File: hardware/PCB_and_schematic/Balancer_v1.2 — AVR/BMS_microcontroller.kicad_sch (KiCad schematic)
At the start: 60 parts, among them J10 RS485, J2 VOLTAGE_3WIRE, J8 ICP, J9 RS485, Q17 BC817, Q19 BC817, Q20 BC817, Q21 BC817, Q22 BC817, U4 TL432DBZ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

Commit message: Add PWM code
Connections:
- net TEMP_HEAT_SINK_12V renamed DAC
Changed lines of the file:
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@@
 		)
 	)
-	(global_label "TEMP_HEAT_SINK_12V"
+	(global_label "DAC"
 		(shape input)
 		(at 72.39 86.36 180)
@@
 		)
 		(property "Intersheetrefs" "${INTERSHEET_REFS}"
-			(at 49.2059 86.36 0)
+			(at 65.7762 86.36 0)
 			(effects
 				(font

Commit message: New schematic BMS
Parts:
- added C4: 100n, Capacitor_SMD:C_0805_2012Metric_Pad1.18x1.45mm_HandSolder, symbol Device:C
- added R12: 10k, Resistor_SMD:R_0805_2012Metric_Pad1.20x1.40mm_HandSolder, symbol Device:R
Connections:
- net +5V: now also C4.1, R12.1
- net UPDI: now also C4.2, R12.2
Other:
- moved on the sheet: C19, C22, C23, J8, R47, R94, U4

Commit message: Update electrical schematic and BMS schematic
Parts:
- removed J8: ICP, Connector_PinHeader_2.54mm:PinHeader_1x06_P2.54mm_Vertical, symbol Connector_Generic:Conn_01x06
- added J16: ICP, Connector_PinHeader_2.54mm:PinHeader_1x05_P2.54mm_Vertical, symbol Connector_Generic:Conn_01x05
- added Q23: BC817, Package_TO_SOT_SMD:SOT-23, symbol Transistor_BJT:BC817
- added R42, R64: 1k, Resistor_SMD:R_0805_2012Metric_Pad1.20x1.40mm_HandSolder, symbol Device:R
- added R65: 4k7, Resistor_SMD:R_0805_2012Metric_Pad1.20x1.40mm_HandSolder, symbol Device:R
- added U10: PC817, Package_DIP:DIP-4_W7.62mm, symbol Isolator:PC817
- added U5: ADUM3211ARZ, R_8_ADI, symbol My-Lib:ADUM3211ARZ
- added U9: B0505S-1W, My-Footprints:B0505S, symbol My-Lib:B0505S-1W
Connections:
- net +5V: now also J16.2 (Pin_2), U10.1, U5.1 (VDD1), U9.1 (GND); no longer J10.1 (Pin_1), J9.1 (Pin_1), R51.1, U6.8 (VCC)
- net DBG_UART: now also J16.5 (Pin_5)
- net GND: now also J16.3 (Pin_3), Q23.2 (E), U5.4 (GND1), U9.2 (VIN); no longer C20.2, D16.1 (A1), D17.1 (A1), J10.4 (Pin_4), J9.4 (Pin_4), R53.2, U6.5 (GND)
- net RS232_RX: now also U5.2 (VOA); no longer U6.1 (RO)
- net RS232_TX: now also U5.3 (VIB); no longer U6.4 (DI)
- net RS485_OUTPUT_ENABLE: now also R64.1; no longer U6.2 (~{RE}), U6.3 (DE)
- net RST: now also J16.1 (Pin_1)
- net UPDI: now also J16.4 (Pin_4)
- new net: Q23.1 (B), R64.2
- new net: Q23.3 (C), R42.1
- new net: R65.2, U10.4, U6.2 (~{RE}), U6.3 (DE)
- new net: U5.7 (VIA), U6.1 (RO)
- new net: U5.6 (VOB), U6.4 (DI)
- new net: R42.2, U10.2
- new net +5V_RS485: J10.1 (Pin_1), J9.1 (Pin_1), R51.1, R65.1, U5.8 (VDD2), U6.8 (VCC), U9.4 (VOUT)
- new net GND_RS485: C20.2, D16.1 (A1), D17.1 (A1), J10.4 (Pin_4), J9.4 (Pin_4), R53.2, U10.3, U5.5 (GND2), U6.5 (GND), U9.3 (0V)
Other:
- moved on the sheet: C17, C18, C20, C21, C24, C25, D15, D16, D17, D18, D19, D20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

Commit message: Balancer PCB update
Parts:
- added C32: 100n, Capacitor_SMD:C_0805_2012Metric_Pad1.18x1.45mm_HandSolder, symbol Device:C
- U5: footprint R_8_ADI -> Package_SO:SO-8_3.9x4.9mm_P1.27mm
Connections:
- net +5V: no longer C20.1
- net +5V_RS485: now also C20.1, C32.1
- net GND_RS485: now also C32.2
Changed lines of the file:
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@@
 	)
 	(symbol
+		(lib_id "Device:C")
+		(at 273.05 102.87 0)
+		(unit 1)
+		(exclude_from_sim no)
+		(in_bom yes)
+		(on_board yes)
+		(dnp no)
+		(property "Reference" "C32"
+			(at 265.43 101.854 0)
+			(effects
+				(font
+					(size 1.27 1.27)
+				)
+				(justify left)
+			)
+		)
+		(property "Value" "100n"
+			(at 265.43 104.14 0)
+			(effects
+				(font
+					(size 1.27 1.27)
+				)
+				(justify left)
+			)
+		)
+		(property "Footprint" "Capacitor_SMD:C_0805_2012Metric_Pad1.18x1.45mm_HandSolder"
+			(at 274.0152 106.68 0)
+			(effects
+				(font
+					(size 1.27 1.27)
+				)
+				(hide yes)
+			)
+		)
+		(property "Datasheet" "~"
+			(at 273.05 102.87 0)
+			(effects
+				(font
+					(size 1.27 1.27)
+				)
+				(hide yes)
+			)
+		)
+		(property "Description" "Unpolarized capacitor"
+			(at 273.05 102.87 0)
+			(effects
+				(font
+					(size 1.27 1.27)
+				)
+				(hide yes)
+			)
+		)
+		(pin "2"
+		)
+		(pin "1"
+		)
+		(instances
+			(project "Balancer"
+				(path "/555ba40f-9abb-4b99-82c6-07e888fda9fd/3b90ff07-e5cb-404b-939d-de320e975ba1"
+					(reference "C32")
+					(unit 1)
+				)
+			)
+		)
+	)
+	(symbol
 		(lib_id "Device:R")
 		(at 34.29 123.19 0)
@@
 	)
 	(symbol
+		(lib_id "power:+5V")
+		(at 273.05 74.93 0)
+		(unit 1)
+		(exclude_from_sim no)
+		(in_bom yes)
+		(on_board yes)
+		(dnp no)
+		(fields_autoplaced yes)
+		(property "Reference" "#PWR072"
+			(at 273.05 78.74 0)
+			(effects
+				(font
+					(size 1.27 1.27)
+				)
+				(hide yes)
+			)
+		)
+		(property "Value" "+5V_RS485"
+			(at 273.05 69.85 0)
+			(effects
+				(font
+					(size 1.27 1.27)
+				)
+			)
+		)
+		(property "Footprint" ""
+			(at 273.05 74.93 0)
+			(effects
+				(font
+					(size 1.27 1.27)
+				)
+				(hide yes)
+			)
+		)
+		(property "Datasheet" ""
+			(at 273.05 74.93 0)
+			(effects
+				(font
+					(size 1.27 1.27)
+				)
+				(hide yes)
+			)
+		)
+		(property "Description" "Power symbol creates a global label with name \"+5V\""
+			(at 273.05 74.93 0)
+			(effects
+				(font
+					(size 1.27 1.27)
+				)
+				(hide yes)
+			)
+		)
+		(pin "1"
+		)
+		(instances
+			(project "Balancer"
+				(path "/555ba40f-9abb-4b99-82c6-07e888fda9fd/3b90ff07-e5cb-404b-939d-de320e975ba1"
+					(reference "#PWR072")
+					(unit 1)
+				)
+			)
+		)
+	)
+	(symbol
 		(lib_id "My-Lib:ADUM3211ARZ")
 		(at 219.71 54.61 0)
@@
 			)
 		)
-		(property "Footprint" "R_8_ADI"
+		(property "Footprint" "Package_SO:SO-8_3.9x4.9mm_P1.27mm"
 			(at 223.266 53.34 0)
 			(effects
@@
 	)
 	(symbol
-		(lib_id "power:+5V")
-		(at 273.05 74.93 0)
-		(unit 1)
-		(exclude_from_sim no)
-		(in_bom yes)
-		(on_board yes)
-		(dnp no)
-		(fields_autoplaced yes)
-		(property "Reference" "#PWR072"
-			(at 273.05 78.74 0)
-			(effects
-				(font
-					(size 1.27 1.27)
-				)
-				(hide yes)
-			)
-		)
-		(property "Value" "+5V"
-			(at 273.05 69.85 0)
-			(effects
-				(font
-					(size 1.27 1.27)
-				)
-			)
-		)
-		(property "Footprint" ""
-			(at 273.05 74.93 0)
-			(effects
-				(font
-					(size 1.27 1.27)
-				)
-				(hide yes)
-			)
-		)
-		(property "Datasheet" ""
-			(at 273.05 74.93 0)
-			(effects
-				(font
-					(size 1.27 1.27)
-				)
-				(hide yes)
-			)
-		)
-		(property "Description" "Power symbol creates a global label with name \"+5V\""
-			(at 273.05 74.93 0)
-			(effects
-				(font
-					(size 1.27 1.27)
-				)
-				(hide yes)
-			)
-		)
-		(pin "1"
-		)
-		(instances
-			(project "Balancer"
-				(path "/555ba40f-9abb-4b99-82c6-07e888fda9fd/3b90ff07-e5cb-404b-939d-de320e975ba1"
-					(reference "#PWR072")
-					(unit 1)
-				)
-			)
-		)
-	)
-	(symbol
 		(lib_id "Transistor_BJT:BC817")
 		(at 104.14 384.81 0)
@@
 	(symbol
 		(lib_id "power:GND")
+		(at 273.05 106.68 0)
+		(unit 1)
+		(exclude_from_sim no)
+		(in_bom yes)
+		(on_board yes)
+		(dnp no)
+		(fields_autoplaced yes)
+		(property "Reference" "#PWR0115"
+			(at 273.05 113.03 0)
+			(effects
+				(font
+					(size 1.27 1.27)
+				)
+				(hide yes)
+			)
+		)
+		(property "Value" "GND_RS485"
+			(at 273.05 111.76 0)
+			(effects
+				(font
+					(size 1.27 1.27)
+				)
+			)
+		)
+		(property "Footprint" ""
+			(at 273.05 106.68 0)
+			(effects
+				(font
+					(size 1.27 1.27)
+				)
+				(hide yes)
+			)
+		)
+		(property "Datasheet" ""
+			(at 273.05 106.68 0)
+			(effects
+				(font
+					(size 1.27 1.27)
+				)
+				(hide yes)
+			)
+		)
+		(property "Description" "Power symbol creates a global label with name \"GND\" , ground"
+			(at 273.05 106.68 0)
+			(effects
+				(font
+					(size 1.27 1.27)
+				)
+				(hide yes)
+			)
+		)
+		(pin "1"
+		)
+		(instances
+			(project "Balancer"
+				(path "/555ba40f-9abb-4b99-82c6-07e888fda9fd/3b90ff07-e5cb-404b-939d-de320e975ba1"
+					(reference "#PWR0115")
+					(unit 1)
+				)
+			)
+		)
+	)
+	(symbol
+		(lib_id "power:GND")
 		(at 90.17 374.65 0)
 		(unit 1)
@@
 					(unit 1)
 				)
+			)
+		)
+	)
+	(symbol
+		(lib_id "power:+5V")
+		(at 273.05 99.06 0)
+		(unit 1)
+		(exclude_from_sim no)
+		(in_bom yes)
+		(on_board yes)
+		(dnp no)
+		(fields_autoplaced yes)
+		(property "Reference" "#PWR0114"
+			(at 273.05 102.87 0)
+			(effects
+				(font
+					(size 1.27 1.27)
+				)
+				(hide yes)
+			)
+		)
+		(property "Value" "+5V_RS485"
+			(at 273.05 93.98 0)
+			(effects
+				(font
+					(size 1.27 1.27)
+				)
+			)
+		)
+		(property "Footprint" ""
+			(at 273.05 99.06 0)
+			(effects
+				(font
+					(size 1.27 1.27)
+				)
+				(hide yes)
+			)
+		)
+		(property "Datasheet" ""
+			(at 273.05 99.06 0)
+			(effects
+				(font
+					(size 1.27 1.27)
+				)
+				(hide yes)
+			)
+		)
+		(property "Description" "Power symbol creates a global label with name \"+5V\""
+			(at 273.05 99.06 0)
+			(effects
+				(font
+					(size 1.27 1.27)
+				)
+				(hide yes)
+			)
+		)
+		(pin "1"
+		)
+		(instances
+			(project "Balancer"
+				(path "/555ba40f-9abb-4b99-82c6-07e888fda9fd/3b90ff07-e5cb-404b-939d-de320e975ba1"
+					(reference "#PWR0114")
+					(unit 1)
+				)

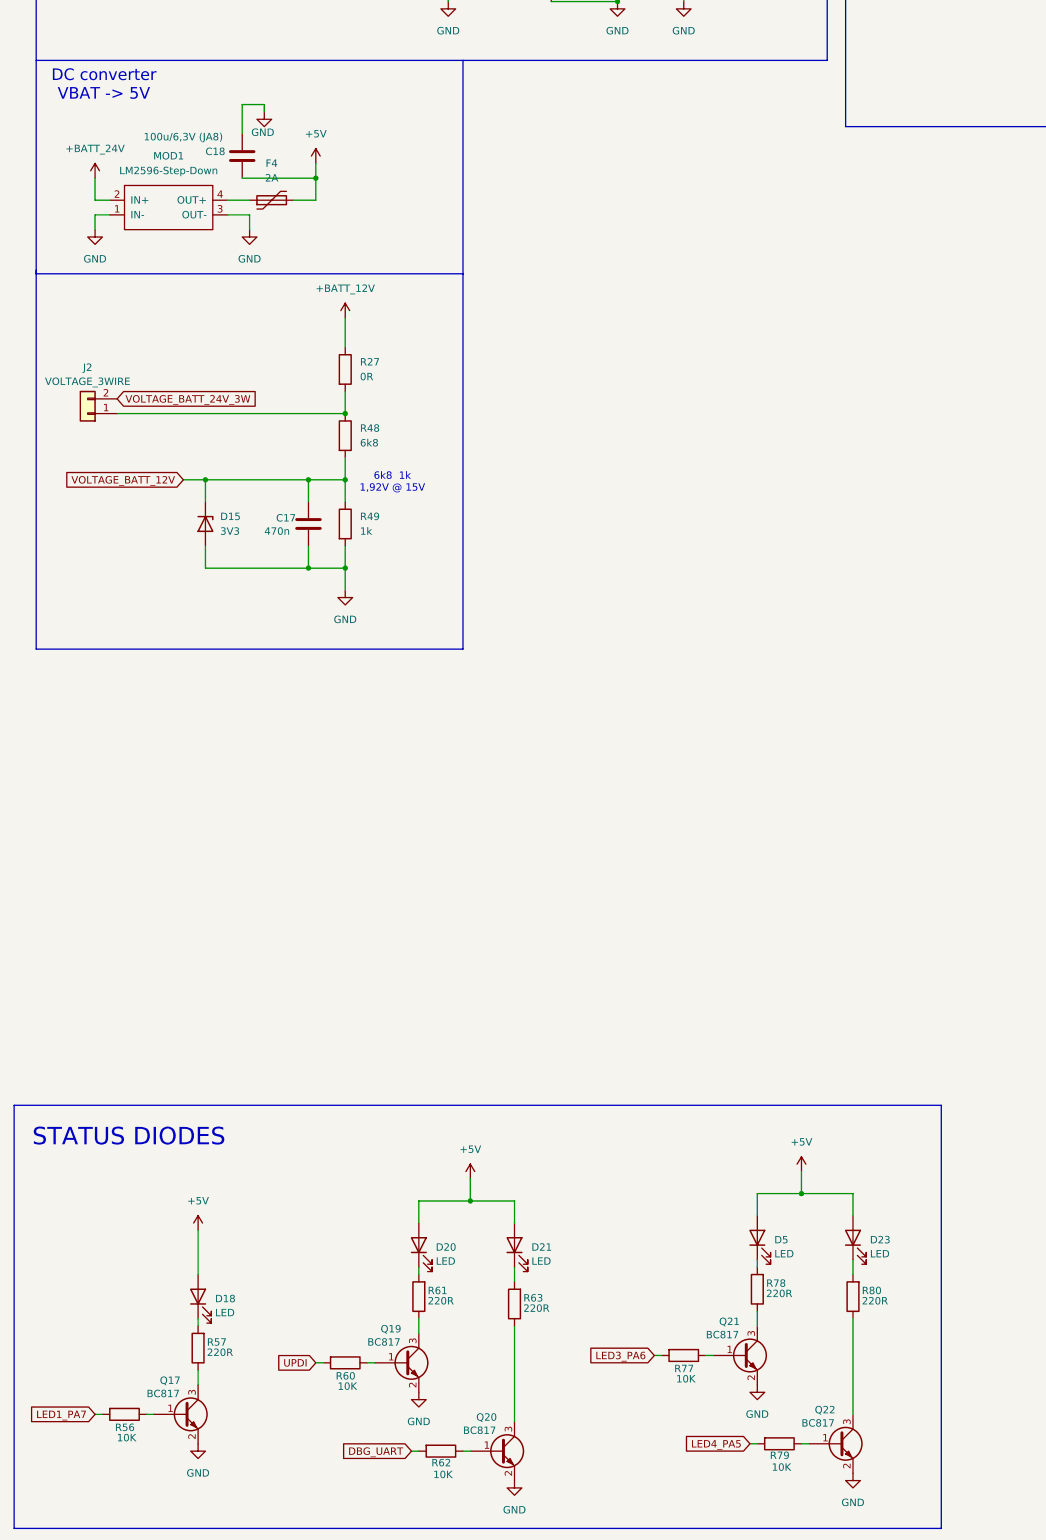
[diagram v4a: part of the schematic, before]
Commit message: Balancer PCB routing
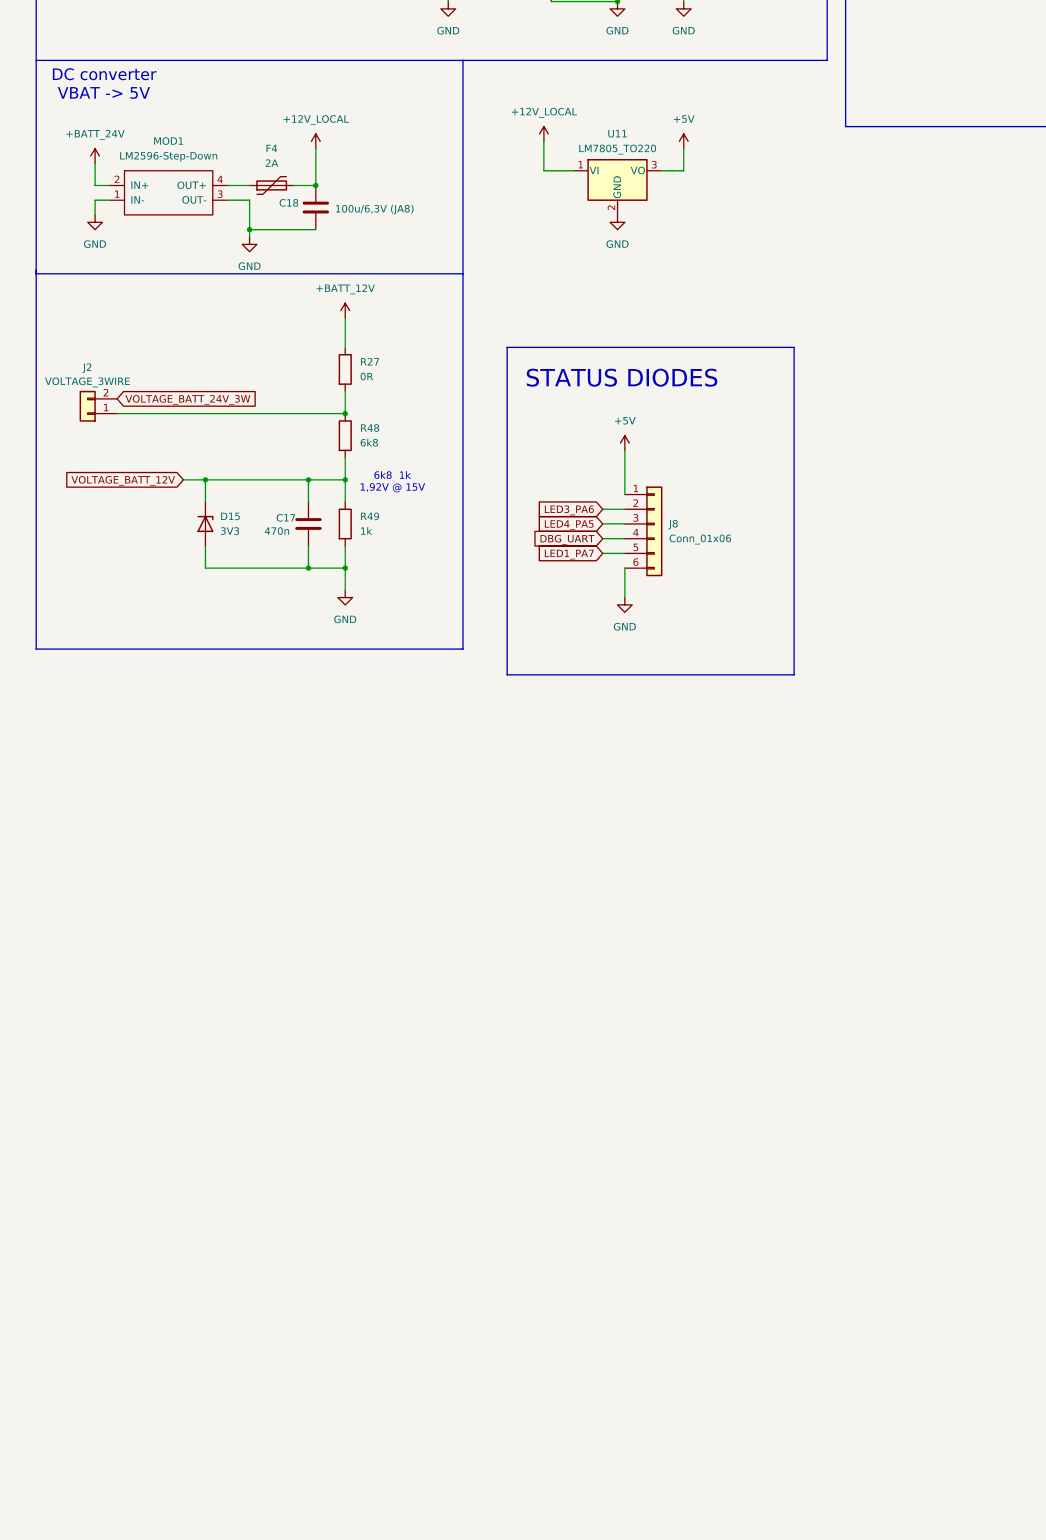
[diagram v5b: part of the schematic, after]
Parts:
- removed D18, D20, D21: LED, LED_THT:LED_D5.0mm, symbol Device:LED
- removed D23, D5: LED, LED_SMD:LED_PLCC-2_3.4x3.0mm_KA, symbol Device:LED
- removed Q17, Q19, Q20, Q21, Q22: BC817, Package_TO_SOT_SMD:SOT-23, symbol Transistor_BJT:BC817
- removed R56, R60, R62, R77, R79: 10K, Resistor_SMD:R_0805_2012Metric_Pad1.20x1.40mm_HandSolder, symbol Device:R
- removed R57, R61, R63, R78, R80: 220R, Resistor_SMD:R_0805_2012Metric_Pad1.20x1.40mm_HandSolder, symbol Device:R
- added J8: Conn_01x06, My-Footprints-connectors:JST_XH_1x06_P2.54mm_Vertical, symbol Connector_Generic:Conn_01x06
- added U11: LM7805_TO220, Package_TO_SOT_THT:TO-220-3_Vertical, symbol Regulator_Linear:LM7805_TO220
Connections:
- net +5V: now also J8.1 (Pin_1), U11.3 (VO); no longer C18.2, F4.2
- net DBG_UART: now also J8.4 (Pin_4)
- net GND: now also C18.2, J8.6 (Pin_6), U11.2 (GND); no longer C18.1
- net LED1_PA7: now also J8.5 (Pin_5)
- net LED3_PA6: now also J8.2 (Pin_2)
- net LED4_PA5: now also J8.3 (Pin_3)
- new net +12V_LOCAL: C18.1, F4.2, U11.1 (VI)
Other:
- moved on the sheet: C18, F4, MOD1
